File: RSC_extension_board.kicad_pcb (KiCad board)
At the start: 2 copper layers, 65 x 56 mm, 102 parts, among them IC1 LM34936RHFR, J1 Conn_01x02, J10 Conn_01x03, J11 Conn_01x10, J14 USB_C_Receptacle_PowerOnly_6P, J2 Raspberry_Pi_4, J3 Conn_01x02, J4 Conn_01x03, J5 Conn_01x03, J6 Conn_01x03, J7 PRT-14417, J8 Conn_01x04, J9 Conn_01x03, Q1 2N7002-7-F, Q2 BSS138, Q3 CSD17571Q2, Q4 CSD17571Q2, Q5 CSD15571Q2, Q6 CSD15571Q2, Q7 CSD15571Q2, Q8 BSC084P03NS3GATMA1, Q9 BSC084P03NS3GATMA1, U3 CYPD3177-24LQ

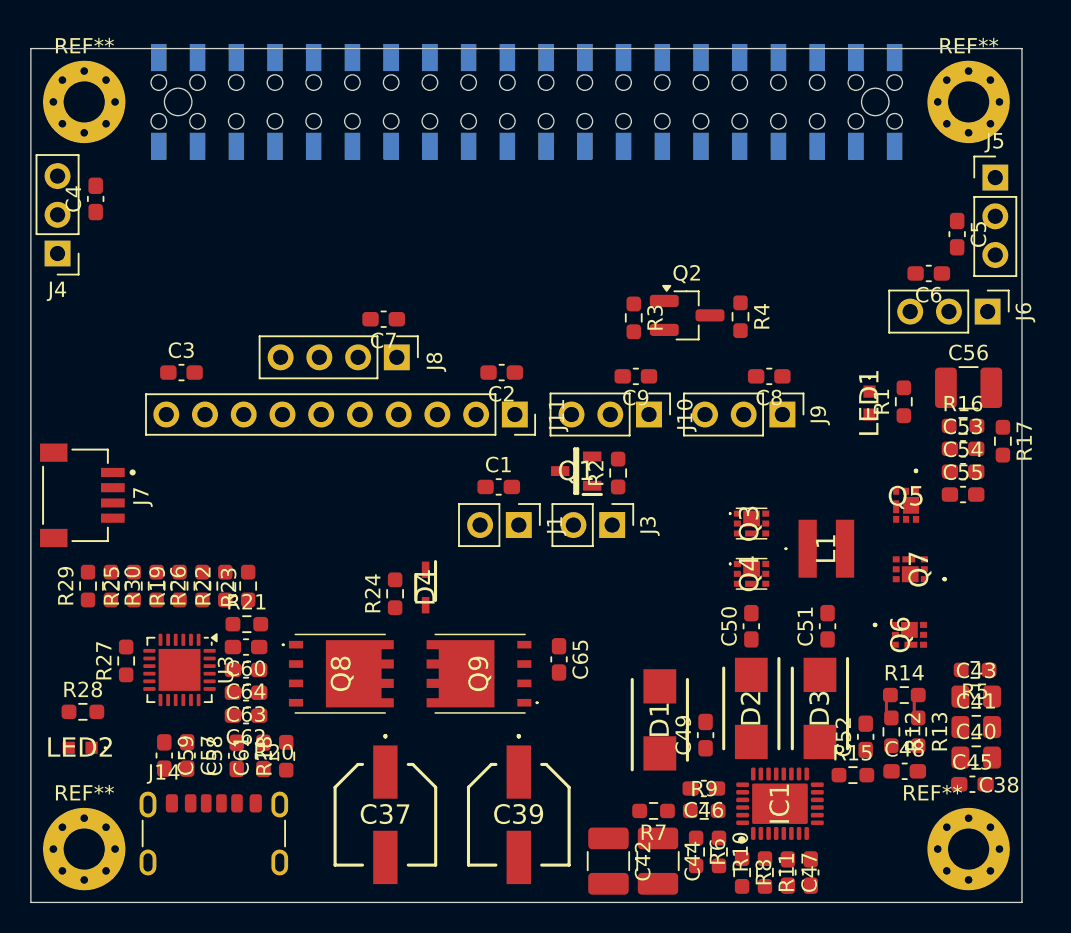
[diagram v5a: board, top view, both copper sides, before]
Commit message: rounded edges, new rules
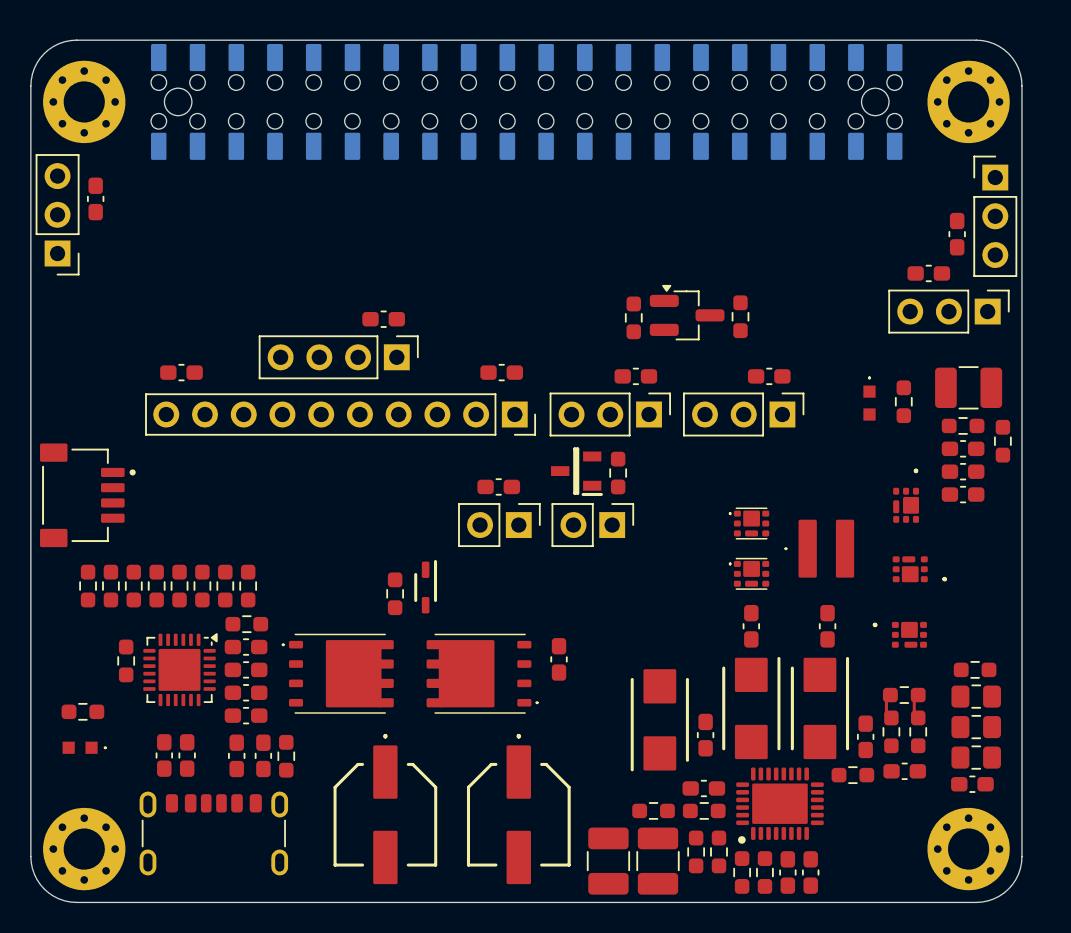
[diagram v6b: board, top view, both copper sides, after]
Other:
- board size 65 x 56 mm -> 65 x 56.5 mm

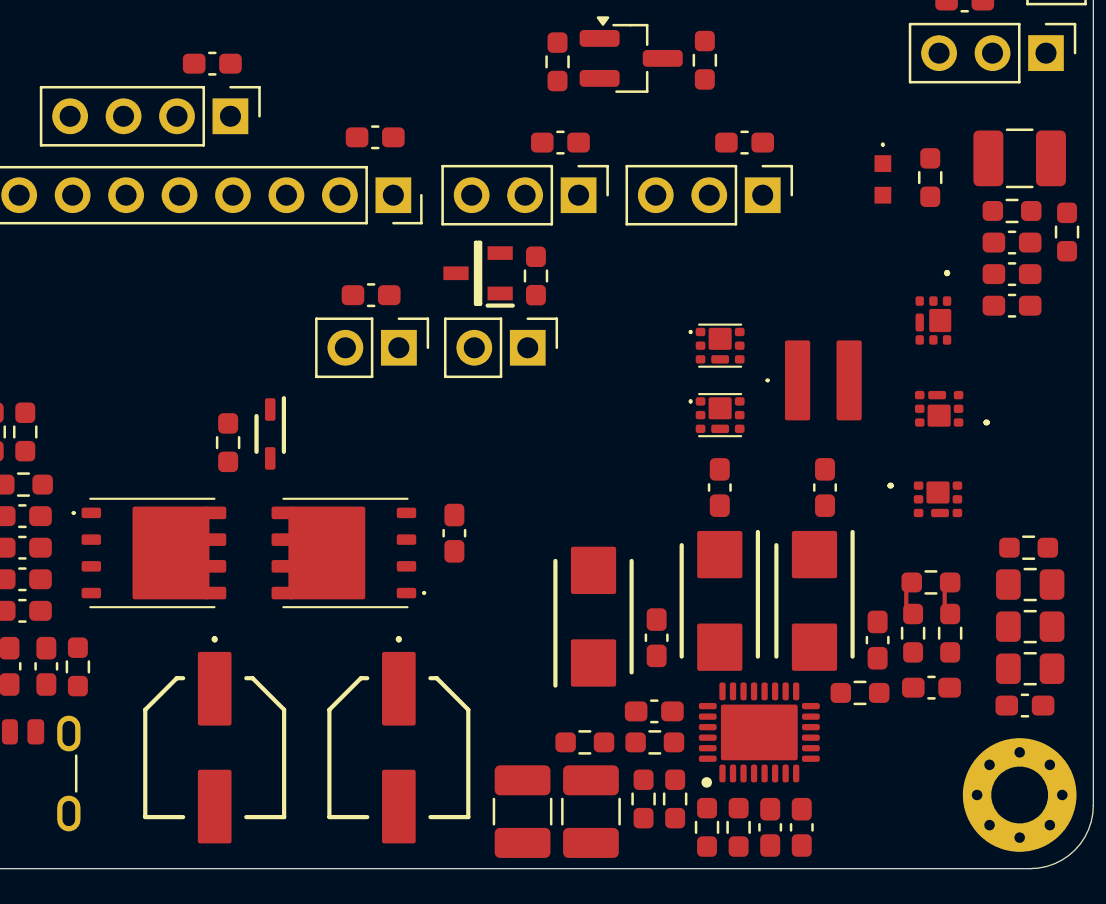
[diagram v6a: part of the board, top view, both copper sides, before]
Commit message: added fuze
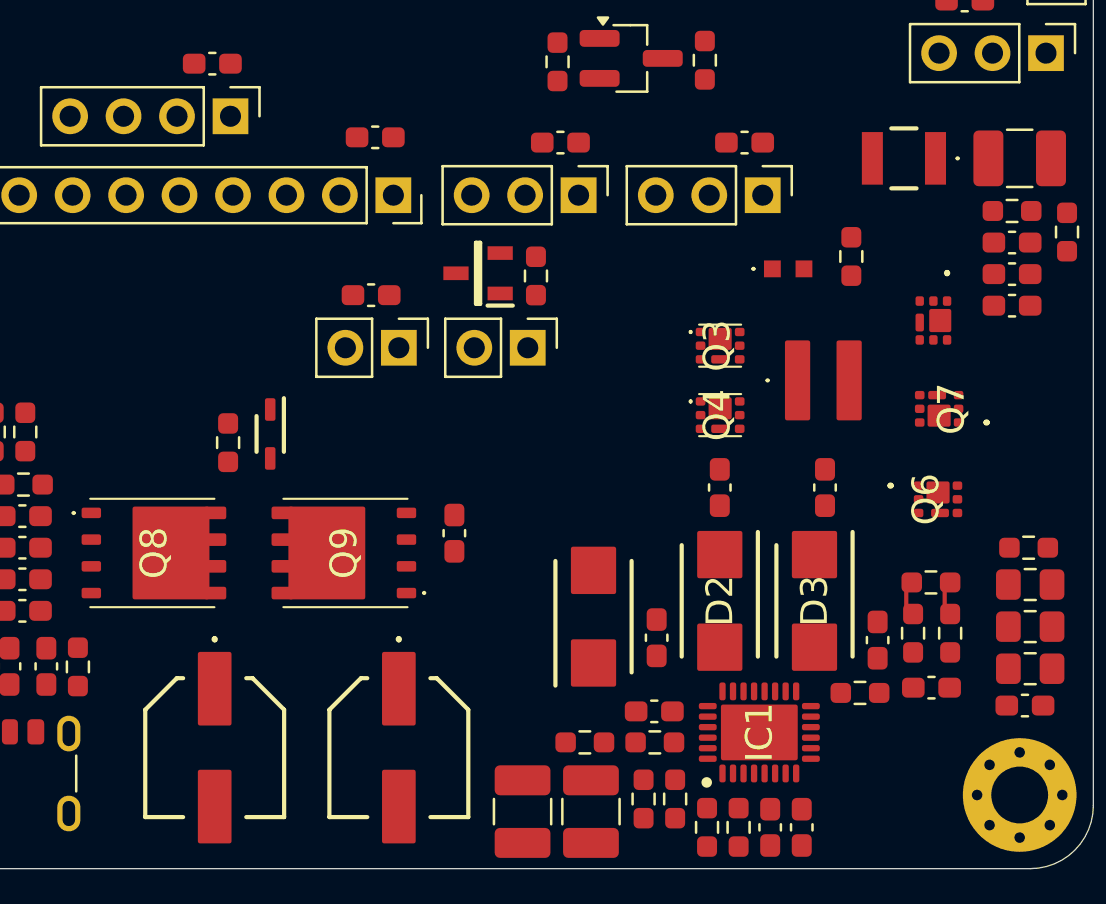
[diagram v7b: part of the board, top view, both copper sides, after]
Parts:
- added F1: PTSLR12106V700, PTSLR12106V700:PTSLR12106V700, F.Cu at (151.0, 67.2)
- moved LED1 6.19 mm to (145.5, 72.5), turned to 0 degrees
- moved R1 5.30 mm to (148.5, 71.9)
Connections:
- C53 pad 1: +5V -> Net-(IC1-VOSNS)
- C54 pad 1: +5V -> Net-(IC1-VOSNS)
- C55 pad 1: +5V -> Net-(IC1-VOSNS)
- C56 pad 1: +5V -> Net-(IC1-VOSNS)
- IC1 pad 9: +5V -> Net-(IC1-VOSNS)
- Q5 pad 1: +5V -> Net-(IC1-VOSNS)
- Q5 pad 2: +5V -> Net-(IC1-VOSNS)
- Q5 pad 5: +5V -> Net-(IC1-VOSNS)
- Q5 pad 6: +5V -> Net-(IC1-VOSNS)
- Q5 pad 7: +5V -> Net-(IC1-VOSNS)
- Q7 pad 1: +5V -> Net-(IC1-VOSNS)
- Q7 pad 2: +5V -> Net-(IC1-VOSNS)
- Q7 pad 5: +5V -> Net-(IC1-VOSNS)
- Q7 pad 6: +5V -> Net-(IC1-VOSNS)
- Q7 pad 7: +5V -> Net-(IC1-VOSNS)
- R16 pad 1: +5V -> Net-(IC1-VOSNS)

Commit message: added pi and piZero(or voice hat) outlines
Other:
- board text added: "B+"
- board text added: "Zero"
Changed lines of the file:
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@@
 		)
+	)
+	(gr_rect
+		(start 95 45)
+		(end 180 101)
+		(stroke
+			(width 0.2)
+			(type dash)
+		)
+		(fill no)
+		(locked yes)
+		(layer "Dwgs.User")
+	)
+	(gr_rect
+		(start 95 45)
+		(end 160 75)
+		(stroke
+			(width 0.2)
+			(type dash)
+		)
+		(fill no)
+		(locked yes)
+		(layer "Dwgs.User")
 	)
 	(gr_arc
@@
 		(layer "Edge.Cuts")
 	)
+	(gr_text "Zero"
+		(locked yes)
+		(at 158 74.5 0)
+		(layer "Dwgs.User")
+		(effects
+			(font
+				(size 1 1)
+				(thickness 0.15)
+			)
+			(justify bottom)
+		)
+	)
+	(gr_text "B+"
+		(locked yes)
+		(at 178.5 100.5 0)
+		(layer "Dwgs.User")
+		(effects
+			(font
+				(size 1 1)
+				(thickness 0.15)
+			)
+			(justify bottom)
+		)
+	)
 	(segment
